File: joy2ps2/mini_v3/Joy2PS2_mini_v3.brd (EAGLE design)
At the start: 25.4 x 47 mm, 8 parts, among them IC1 ATMEGA168PROUND, Q1 BS170

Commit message: Add files via upload
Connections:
- net KB_DATA: now also Q1.S; no longer Q1.D
- net KB_DATA': now also Q1.D; no longer Q1.S
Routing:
- net +5V: track 80.4 -> 94.8 mm, vias 3 -> 2
- net A4: track 62.4 -> 50.9 mm, vias 0 -> 3
- net GND: track 89.8 -> 99.8 mm
- net A5: track 53.1 -> 45.2 mm, vias 4 -> 3
- net KB_DATA: track 75.4 -> 68.1 mm
- net KB_DATA': track 30.1 -> 23.9 mm
- net A0: track 36.0 -> 40.0 mm, vias 1 -> 0
- net D3: track 44.1 -> 40.2 mm, vias 1 -> 0
- net D2: track 41.8 -> 44.4 mm, vias 0 -> 3
- net D11: track 18.2 -> 16.3 mm
- net D4: track 35.0 -> 33.1 mm
- net D12: track 34.3 -> 35.4 mm
- net RST: track 37.8 -> 36.8 mm, vias 0 -> 1
- net D5: track 21.1 -> 21.8 mm

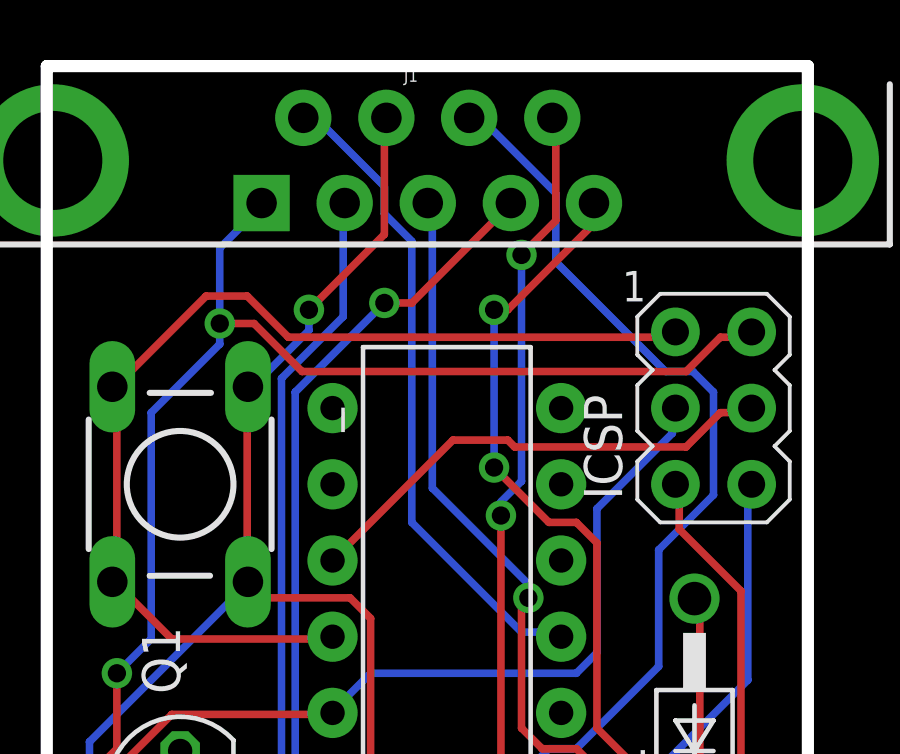
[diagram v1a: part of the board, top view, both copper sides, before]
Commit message: Arcade version
Serigrafías para conexión tipo DB15 Neogeo
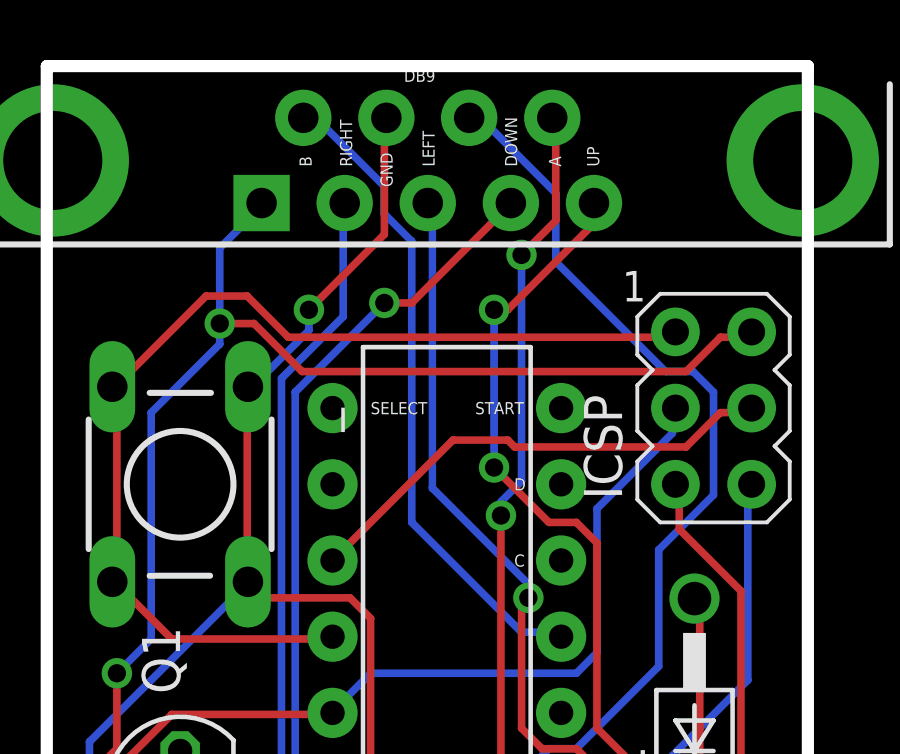
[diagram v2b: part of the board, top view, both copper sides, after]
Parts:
- renumbered J1 to DB9
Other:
- board text added: "A"
- board text added: "B"
- board text added: "C"
- board text added: "D"
- board text added: "DOWN"
- board text added: "LEFT"
- board text added: "RIGHT"
- board text added: "SELECT"
- board text added: "START"
- board text added: "UP"
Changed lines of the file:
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@@
 <text x="14.605" y="23.495" size="1.016" layer="21" rot="R90">PS2_MALE</text>
 <text x="-3.175" y="22.225" size="1.016" layer="21" rot="R90">PS2_FEMALE</text>
+<text x="5.715" y="49.325" size="0.4064" layer="21">SELECT</text>
+<text x="9.2" y="49.325" size="0.4064" layer="21">START</text>
+<text x="13.335" y="57.58" size="0.4064" layer="21" rot="R90">UP</text>
+<text x="12.065" y="57.58" size="0.4064" layer="21" rot="R90">A</text>
+<text x="3.75" y="57.58" size="0.4064" layer="21" rot="R90">B</text>
+<text x="10.6" y="57.58" size="0.4064" layer="21" rot="R90">DOWN</text>
+<text x="7.85" y="57.58" size="0.4064" layer="21" rot="R90">LEFT</text>
+<text x="6.45" y="56.9" size="0.4064" layer="21" rot="R90">GND</text>
+<text x="5.1" y="57.58" size="0.4064" layer="21" rot="R90">RIGHT</text>
+<text x="10.5" y="44.245" size="0.4064" layer="21">C</text>
+<text x="10.5" y="46.785" size="0.4064" layer="21">D</text>
 </plain>
 <attributes>
@@
 <elements>
 <element name="_" library="GeekAmmo" package="TAC-SWITCH-PTH" value="TACTILE-SWITCH-PTH" x="-0.635" y="46.99" rot="R270"/>
-<element name="J1" library="SparkFun-Connectors" package="DB9_MALE" value="" x="7.62" y="57.785">
+<element name="DB9" library="SparkFun-Connectors" package="DB9_MALE" value="" x="7.62" y="57.785">
 <attribute name="PROD_ID" value="CONN-09904" x="7.62" y="57.785" size="1.778" layer="27" display="off"/>
 </element>
@@
 <contactref element="_" pad="1"/>
 <contactref element="_" pad="2"/>
-<contactref element="J1" pad="8"/>
+<contactref element="DB9" pad="8"/>
 <contactref element="IC1" pad="8"/>
 <contactref element="2" pad="6"/>
@@
 </signal>
 <signal name="D2">
-<contactref element="J1" pad="3"/>
+<contactref element="DB9" pad="3"/>
 <contactref element="IC1" pad="4"/>
 <wire x1="14.1732" y1="24.2316" x2="12.1158" y2="24.2316" width="0.254" layer="1"/>
@@
 </signal>
 <signal name="D3">
-<contactref element="J1" pad="4"/>
+<contactref element="DB9" pad="4"/>
 <contactref element="IC1" pad="5"/>
 <wire x1="6.1722" y1="26.7462" x2="11.8872" y2="26.7462" width="0.254" layer="16"/>
@@
 </signal>
 <signal name="D4">
-<contactref element="J1" pad="6"/>
+<contactref element="DB9" pad="6"/>
 <contactref element="IC1" pad="6"/>
 <wire x1="12.1158" y1="29.9466" x2="12.1158" y2="29.2608" width="0.254" layer="16"/>
@@
 </signal>
 <signal name="D5">
-<contactref element="J1" pad="9"/>
+<contactref element="DB9" pad="9"/>
 <contactref element="IC1" pad="11"/>
 <wire x1="10.7442" y1="42.0624" x2="11.8872" y2="42.0624" width="0.254" layer="16"/>
@@
 </signal>
 <signal name="+5V">
-<contactref element="J1" pad="5"/>
+<contactref element="DB9" pad="5"/>
 <contactref element="IC1" pad="7"/>
 <contactref element="2" pad="5"/>
@@
 </signal>
 <signal name="A5">
-<contactref element="J1" pad="2"/>
+<contactref element="DB9" pad="2"/>
 <contactref element="IC1" pad="28"/>
 <wire x1="4.3434" y1="17.3736" x2="4.3434" y2="16.6878" width="0.254" layer="16"/>
@@
 </signal>
 <signal name="A4">
-<contactref element="J1" pad="1"/>
+<contactref element="DB9" pad="1"/>
 <contactref element="IC1" pad="27"/>
 <wire x1="4.572" y1="19.8882" x2="4.572" y2="19.2024" width="0.254" layer="16"/>
@@
 </signal>
 <signal name="A0">
-<contactref element="J1" pad="7"/>
+<contactref element="DB9" pad="7"/>
 <contactref element="IC1" pad="23"/>
 <wire x1="4.572" y1="30.1752" x2="4.572" y2="29.2608" width="0.254" layer="16"/>
